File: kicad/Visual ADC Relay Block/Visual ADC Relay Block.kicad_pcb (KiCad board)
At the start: 4 copper layers, 32.9 x 50.2 mm, 34 parts, among them J1 Out, J2 In, K1 DIPxx-1Cxx-51x, Q1 P-NMOS, U1 74HCT595, U2 74HC245

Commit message: added probe gnd now silky time
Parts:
- moved D6 0.10 mm to (144.1, 96.8)
- moved D7 0.10 mm to (144.1, 103.1)
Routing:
- net GND: track 53.1 -> 68.1 mm, vias 9 -> 11
- net /CL6: track 18.2 -> 23.1 mm, vias 0 -> 2
- net Net-(D1-Pad1): track 19.5 -> 23.0 mm, vias 0 -> 1
- net /Vout: track 117.7 -> 117.8 mm, vias 1 -> 3
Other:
- board text added: "DAC Bit"

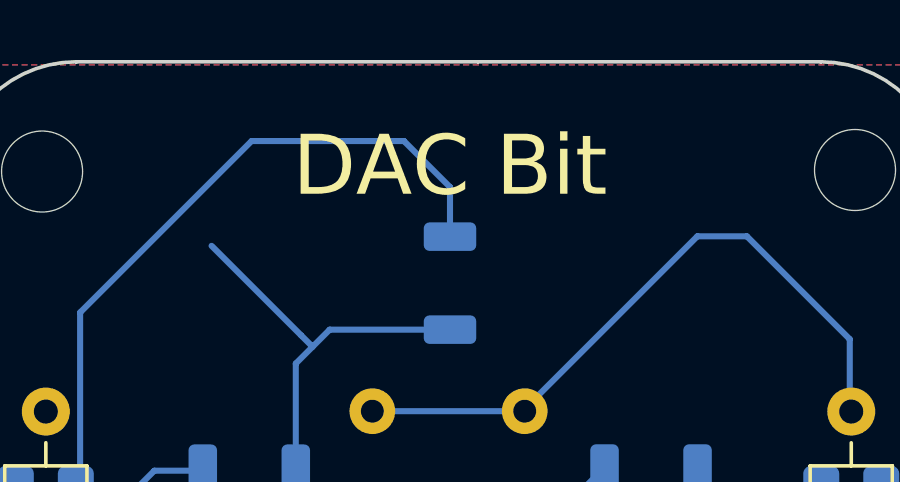
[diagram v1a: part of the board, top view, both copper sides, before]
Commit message: rev1 pre-submit
haven't submitted rev to board house yet
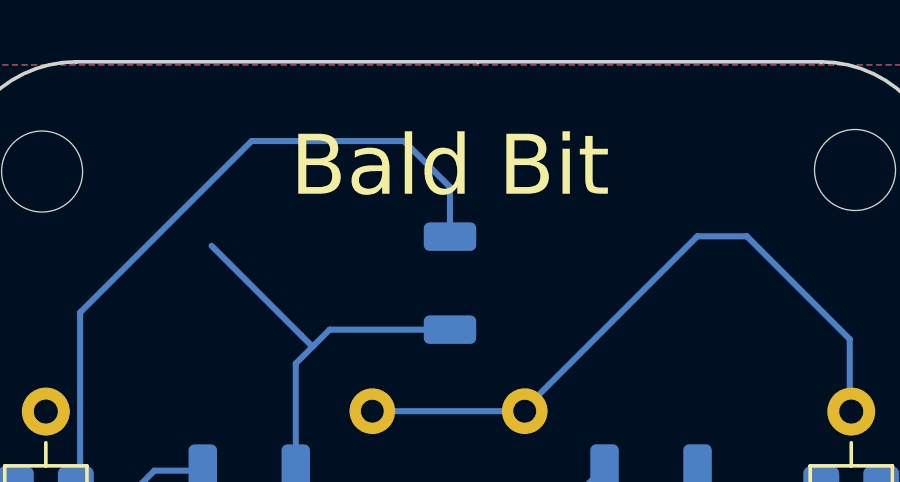
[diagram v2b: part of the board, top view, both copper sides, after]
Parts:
- added REF**: OSHW-Symbol_6.7x6mm_SilkScreen, Symbol:OSHW-Symbol_6.7x6mm_SilkScreen, B.Cu at (137.4, 98.3)
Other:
- board text added: "Bald Bit"
- board text added: "rev 1"
- board text added: "vADC - visualized ADC bald.ee/vadc Thank you for the help chat!"
- board text removed: "DAC Bit"

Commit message: rev1 boards tested
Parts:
- R4, R5, R6, R7, R8, R9: value R -> 330

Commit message: KiCad Notes and Clean-up
Finalized a few details on the schematic. Also created notes for each block based on experience building the boards.
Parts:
- removed REF**: OSHW-Symbol_6.7x6mm_SilkScreen, Symbol:OSHW-Symbol_6.7x6mm_SilkScreen
- Q1: value P-NMOS -> pmv50epear
- R3: value 2R -> 100
